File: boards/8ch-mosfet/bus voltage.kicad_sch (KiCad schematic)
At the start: 6 parts, among them U4 MCP3221A0T

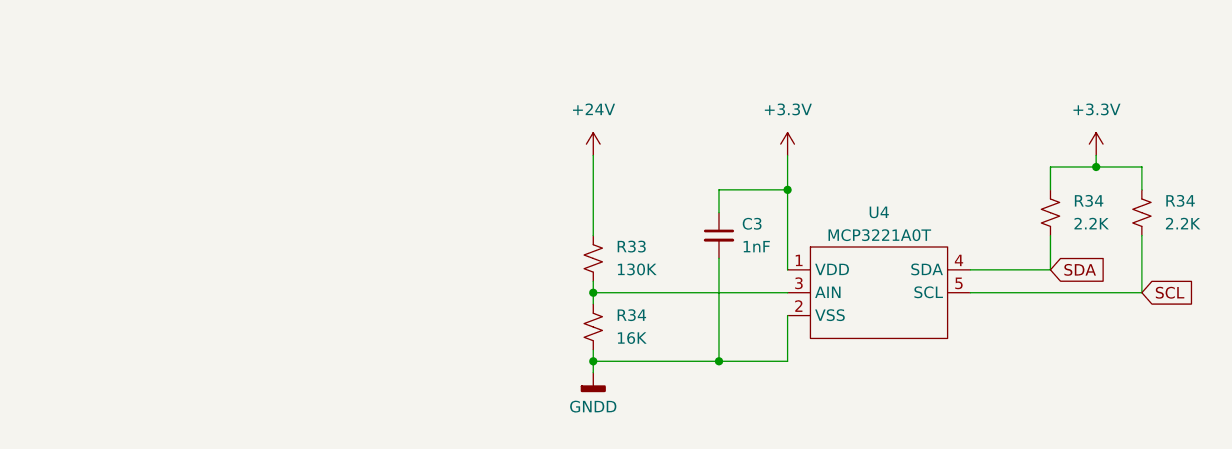
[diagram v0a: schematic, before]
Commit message: updated the adc schematic a bit
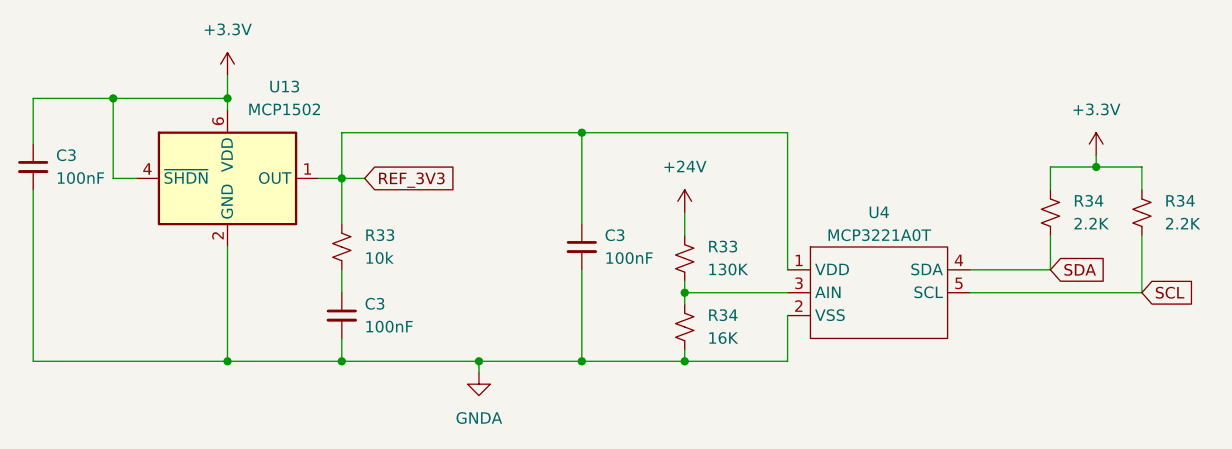
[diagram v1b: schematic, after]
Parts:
- added C3 (x2): 100nF, Capacitor_SMD:C_0805_2012Metric_Pad1.18x1.45mm_HandSolder, symbol Device:C_Small
- added R33: 10k, Resistor_SMD:R_0805_2012Metric_Pad1.20x1.40mm_HandSolder, symbol Device:R_Small_US
- added U13: MCP1502, Package_TO_SOT_SMD:SOT-23-6, symbol Reference_Voltage:MCP1501-30xCH
- C3: value 1nF -> 100nF
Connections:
- net +3.3V: now also C3.1, U13.4 (~{SHDN}), U13.6 (VDD); no longer C3.1, U4.1 (VDD)
- net GNDD renamed GNDA
- net GNDA: now also C3.2, C3.2, U13.2 (GND), U13.3 (GND), U13.5 (GND)
- new net: C3.1, R33.1
- new net REF_3V3: C3.1, R33.2, U13.1 (OUT), U4.1 (VDD)
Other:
- moved on the sheet: C3, R33, R34

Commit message: upgraded the i2c/serial connectors + power based on the sailor hat schematic
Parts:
- removed R34 (x2): 2.2K, Resistor_SMD:R_0805_2012Metric_Pad1.20x1.40mm_HandSolder, symbol Device:R_Small_US
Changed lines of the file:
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@@
   (junction (at 123.19 102.87) (diameter 0) (color 0 0 0 0)
   )
-  (junction (at 168.91 81.28) (diameter 0) (color 0 0 0 0)
-  )
   (junction (at 72.39 102.87) (diameter 0) (color 0 0 0 0)
   )
   (junction (at 72.39 73.66) (diameter 0) (color 0 0 0 0)
   )
-  (junction (at 111.76 77.47) (diameter 0) (color 0 0 0 0)
+  (junction (at 111.76 73.66) (diameter 0) (color 0 0 0 0)
   )
   (junction (at 85.09 102.87) (diameter 0) (color 0 0 0 0)
@@
     (stroke (width 0) (type default))
   )
-  (wire (pts (xy 163.83 81.28) (xy 168.91 81.28))
-    (stroke (width 0) (type default))
-  )
-  (wire (pts (xy 111.76 77.47) (xy 111.76 87.63))
-    (stroke (width 0) (type default))
-  )
   (wire (pts (xy 123.19 95.25) (xy 134.62 95.25))
     (stroke (width 0) (type default))
@@
     (stroke (width 0) (type default))
   )
-  (wire (pts (xy 134.62 77.47) (xy 134.62 92.71))
+  (wire (pts (xy 134.62 73.66) (xy 134.62 92.71))
     (stroke (width 0) (type default))
   )
@@
     (stroke (width 0) (type default))
   )
-  (wire (pts (xy 173.99 83.82) (xy 173.99 81.28))
-    (stroke (width 0) (type default))
-  )
   (wire (pts (xy 85.09 92.71) (xy 85.09 95.25))
     (stroke (width 0) (type default))
@@
     (stroke (width 0) (type default))
   )
-  (wire (pts (xy 163.83 88.9) (xy 163.83 92.71))
-    (stroke (width 0) (type default))
-  )
   (wire (pts (xy 72.39 90.17) (xy 72.39 102.87))
     (stroke (width 0) (type default))
   )
-  (wire (pts (xy 163.83 83.82) (xy 163.83 81.28))
-    (stroke (width 0) (type default))
-  )
   (wire (pts (xy 100.33 102.87) (xy 111.76 102.87))
     (stroke (width 0) (type default))
@@
     (stroke (width 0) (type default))
   )
-  (wire (pts (xy 173.99 88.9) (xy 173.99 95.25))
-    (stroke (width 0) (type default))
-  )
   (wire (pts (xy 72.39 73.66) (xy 59.69 73.66))
     (stroke (width 0) (type default))
@@
     (stroke (width 0) (type default))
   )
-  (wire (pts (xy 154.94 95.25) (xy 173.99 95.25))
+  (wire (pts (xy 154.94 95.25) (xy 158.75 95.25))
     (stroke (width 0) (type default))
   )
@@
     (stroke (width 0) (type default))
   )
-  (wire (pts (xy 111.76 77.47) (xy 134.62 77.47))
+  (wire (pts (xy 111.76 73.66) (xy 134.62 73.66))
     (stroke (width 0) (type default))
   )
@@
     (stroke (width 0) (type default))
   )
-  (wire (pts (xy 85.09 77.47) (xy 111.76 77.47))
-    (stroke (width 0) (type default))
-  )
-  (wire (pts (xy 168.91 81.28) (xy 168.91 80.01))
-    (stroke (width 0) (type default))
-  )
-  (wire (pts (xy 173.99 81.28) (xy 168.91 81.28))
+  (wire (pts (xy 85.09 73.66) (xy 111.76 73.66))
     (stroke (width 0) (type default))
   )
@@
     (stroke (width 0) (type default))
   )
-  (wire (pts (xy 85.09 82.55) (xy 85.09 77.47))
+  (wire (pts (xy 85.09 82.55) (xy 85.09 73.66))
     (stroke (width 0) (type default))
   )
@@
     (stroke (width 0) (type default))
   )
-  (wire (pts (xy 154.94 92.71) (xy 163.83 92.71))
+  (wire (pts (xy 154.94 92.71) (xy 158.75 92.71))
     (stroke (width 0) (type default))
   )
@@
   )
   (wire (pts (xy 59.69 73.66) (xy 50.8 73.66))
+    (stroke (width 0) (type default))
+  )
+  (wire (pts (xy 111.76 73.66) (xy 111.76 87.63))
     (stroke (width 0) (type default))
   )
@@
     )
   )
-  (global_label "SDA" (shape input) (at 163.83 92.71 0) (fields_autoplaced)
+  (global_label "SDA" (shape input) (at 158.75 92.71 0) (fields_autoplaced)
     (effects (font (size 1.27 1.27)) (justify left))
-    (property "Intersheetrefs" "${INTERSHEET_REFS}" (at 170.3833 92.71 0)
+    (property "Intersheetrefs" "${INTERSHEET_REFS}" (at 165.3033 92.71 0)
       (effects (font (size 1.27 1.27)) (justify left) hide)
     )
   )
-  (global_label "SCL" (shape input) (at 173.99 95.25 0) (fields_autoplaced)
+  (global_label "SCL" (shape input) (at 158.75 95.25 0) (fields_autoplaced)
     (effects (font (size 1.27 1.27)) (justify left))
-    (property "Intersheetrefs" "${INTERSHEET_REFS}" (at 180.4828 95.25 0)
+    (property "Intersheetrefs" "${INTERSHEET_REFS}" (at 165.2428 95.25 0)
       (effects (font (size 1.27 1.27)) (justify left) hide)
-    )
-  )
-  (symbol (lib_id "Device:R_Small_US") (at 163.83 86.36 180) (unit 1)
-    (in_bom yes) (on_board yes) (dnp no) (fields_autoplaced)
-    (property "Reference" "R34" (at 166.37 85.09 0)
-      (effects (font (size 1.27 1.27)) (justify right))
-    )
-    (property "Value" "2.2K" (at 166.37 87.63 0)
-      (effects (font (size 1.27 1.27)) (justify right))
-    )
-    (property "Footprint" "Resistor_SMD:R_0805_2012Metric_Pad1.20x1.40mm_HandSolder" (at 163.83 86.36 0)
-      (effects (font (size 1.27 1.27)) hide)
-    )
-    (property "Datasheet" "~" (at 163.83 86.36 0)
-      (effects (font (size 1.27 1.27)) hide)
-    )
-    (property "Vendor" "652-CR0805JW-104ELF" (at 163.83 86.36 0)
-      (effects (font (size 1.27 1.27)) hide)
-    )
-    (pin "1")
-    (pin "2")
-    (instances
-      (project "8ch-mosfet"
-        (path "/c83c6236-96e9-46ad-9d7a-9e2efa4a7966"
-          (reference "R34") (unit 1)
-        )
-        (path "/c83c6236-96e9-46ad-9d7a-9e2efa4a7966/0eec6767-666b-42c0-ba36-2a83c9caeade"
-          (reference "R4") (unit 1)
-        )
-        (path "/c83c6236-96e9-46ad-9d7a-9e2efa4a7966/ccdb1c25-8d0f-4f30-ab70-bbc1ecf3f6f7"
-          (reference "R8") (unit 1)
-        )
-        (path "/c83c6236-96e9-46ad-9d7a-9e2efa4a7966/1e692482-a022-407a-8cb5-d9a3b23521a6"
-          (reference "R12") (unit 1)
-        )
-        (path "/c83c6236-96e9-46ad-9d7a-9e2efa4a7966/5952e660-2bb6-45cf-b9ea-f7a7c2d0954e"
-          (reference "R16") (unit 1)
-        )
-        (path "/c83c6236-96e9-46ad-9d7a-9e2efa4a7966/772d44f5-8758-48db-a140-72ed8e75e88c"
-          (reference "R20") (unit 1)
-        )
-        (path "/c83c6236-96e9-46ad-9d7a-9e2efa4a7966/424e7b24-5644-46f2-85bb-1e459a343705"
-          (reference "R24") (unit 1)
-        )
-        (path "/c83c6236-96e9-46ad-9d7a-9e2efa4a7966/4c1df725-56ca-4be4-8107-a39054acbca4"
-          (reference "R28") (unit 1)
-        )
-        (path "/c83c6236-96e9-46ad-9d7a-9e2efa4a7966/a8a81147-5613-4820-beb3-a7ca76d0db8e"
-          (reference "R32") (unit 1)
-        )
-        (path "/c83c6236-96e9-46ad-9d7a-9e2efa4a7966/b87f80e1-ecbd-4ee0-be26-4b252158928b"
-          (reference "R39") (unit 1)
-        )
-      )
     )
   )
@@
         (path "/c83c6236-96e9-46ad-9d7a-9e2efa4a7966/b87f80e1-ecbd-4ee0-be26-4b252158928b"
           (reference "R41") (unit 1)
-        )
-      )
-    )
-  )
-  (symbol (lib_id "Device:R_Small_US") (at 173.99 86.36 180) (unit 1)
-    (in_bom yes) (on_board yes) (dnp no) (fields_autoplaced)
-    (property "Reference" "R34" (at 176.53 85.09 0)
-      (effects (font (size 1.27 1.27)) (justify right))
-    )
-    (property "Value" "2.2K" (at 176.53 87.63 0)
-      (effects (font (size 1.27 1.27)) (justify right))
-    )
-    (property "Footprint" "Resistor_SMD:R_0805_2012Metric_Pad1.20x1.40mm_HandSolder" (at 173.99 86.36 0)
-      (effects (font (size 1.27 1.27)) hide)
-    )
-    (property "Datasheet" "~" (at 173.99 86.36 0)
-      (effects (font (size 1.27 1.27)) hide)
-    )
-    (property "Vendor" "652-CR0805JW-104ELF" (at 173.99 86.36 0)
-      (effects (font (size 1.27 1.27)) hide)
-    )
-    (pin "1")
-    (pin "2")
-    (instances
-      (project "8ch-mosfet"
-        (path "/c83c6236-96e9-46ad-9d7a-9e2efa4a7966"
-          (reference "R34") (unit 1)
-        )
-        (path "/c83c6236-96e9-46ad-9d7a-9e2efa4a7966/0eec6767-666b-42c0-ba36-2a83c9caeade"
-          (reference "R4") (unit 1)
-        )
-        (path "/c83c6236-96e9-46ad-9d7a-9e2efa4a7966/ccdb1c25-8d0f-4f30-ab70-bbc1ecf3f6f7"
-          (reference "R8") (unit 1)
-        )
-        (path "/c83c6236-96e9-46ad-9d7a-9e2efa4a7966/1e692482-a022-407a-8cb5-d9a3b23521a6"
-          (reference "R12") (unit 1)
-        )
-        (path "/c83c6236-96e9-46ad-9d7a-9e2efa4a7966/5952e660-2bb6-45cf-b9ea-f7a7c2d0954e"
-          (reference "R16") (unit 1)
-        )
-        (path "/c83c6236-96e9-46ad-9d7a-9e2efa4a7966/772d44f5-8758-48db-a140-72ed8e75e88c"
-          (reference "R20") (unit 1)
-        )
-        (path "/c83c6236-96e9-46ad-9d7a-9e2efa4a7966/424e7b24-5644-46f2-85bb-1e459a343705"
-          (reference "R24") (unit 1)
-        )
-        (path "/c83c6236-96e9-46ad-9d7a-9e2efa4a7966/4c1df725-56ca-4be4-8107-a39054acbca4"
-          (reference "R28") (unit 1)
-        )
-        (path "/c83c6236-96e9-46ad-9d7a-9e2efa4a7966/a8a81147-5613-4820-beb3-a7ca76d0db8e"
-          (reference "R32") (unit 1)
-        )
-        (path "/c83c6236-96e9-46ad-9d7a-9e2efa4a7966/b87f80e1-ecbd-4ee0-be26-4b252158928b"
-          (reference "R40") (unit 1)
         )
       )
@@
         )
       )
-    )
-  )
-  (symbol (lib_id "power:+3.3V") (at 168.91 80.01 0) (unit 1)
-    (in_bom yes) (on_board yes) (dnp no) (fields_autoplaced)
-    (property "Reference" "#PWR02" (at 168.91 83.82 0)
-      (effects (font (size 1.27 1.27)) hide)
-    )
-    (property "Value" "+3.3V" (at 168.91 74.93 0)
-      (effects (font (size 1.27 1.27)))
-    )
-    (property "Footprint" "" (at 168.91 80.01 0)
-      (effects (font (size 1.27 1.27)) hide)
-    )
-    (property "Datasheet" "" (at 168.91 80.01 0)
-      (effects (font (size 1.27 1.27)) hide)
-    )
-    (pin "1")
-    (instances
-      (project "8ch-mosfet"
-        (path "/c83c6236-96e9-46ad-9d7a-9e2efa4a7966"
-          (reference "#PWR02") (unit 1)
-        )
-        (path "/c83c6236-96e9-46ad-9d7a-9e2efa4a7966/b87f80e1-ecbd-4ee0-be26-4b252158928b"
-          (reference "#PWR068") (unit 1)
-        )
-      )

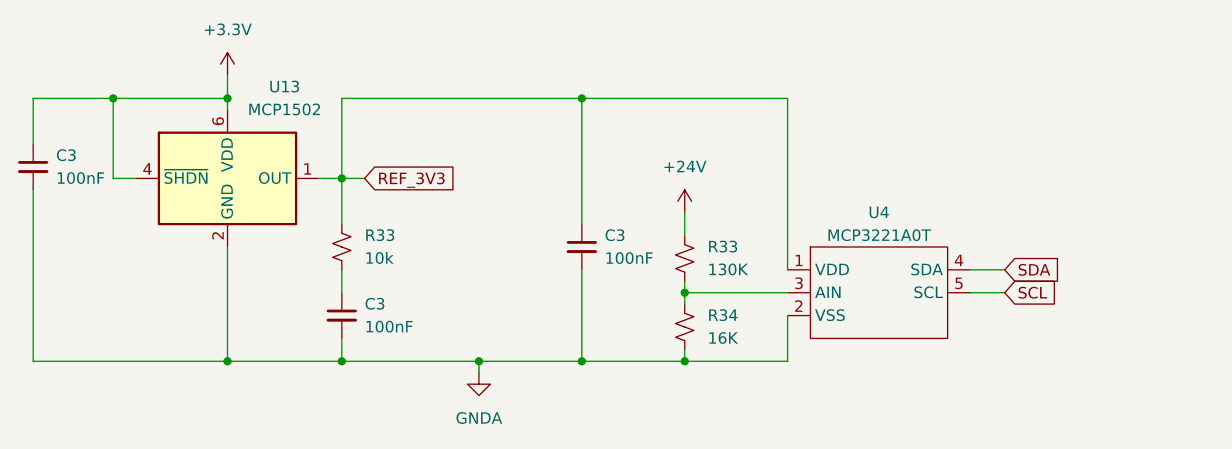
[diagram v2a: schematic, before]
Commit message: silkscreen updated, drc passed.  yay
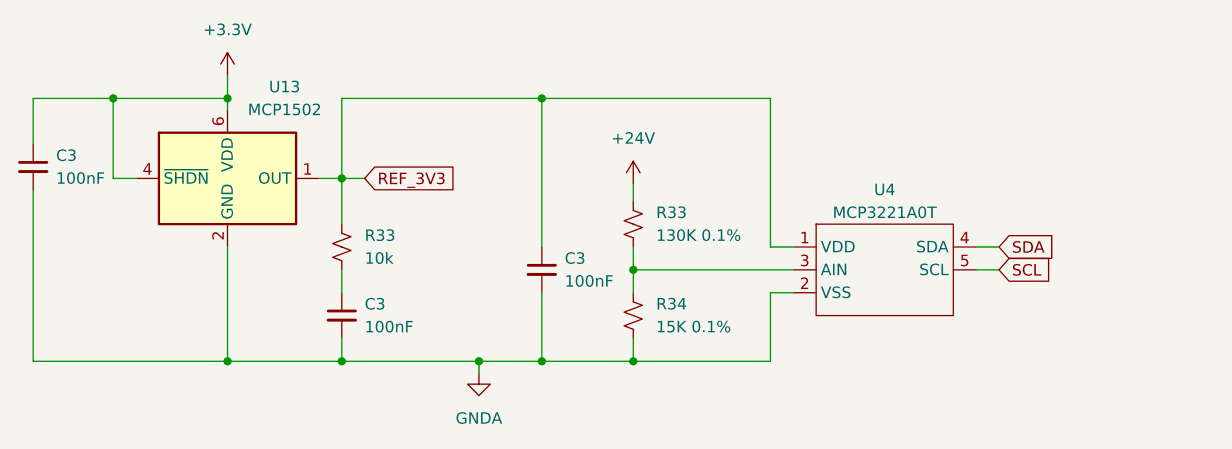
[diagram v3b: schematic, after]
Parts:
- R33: value 130K -> 130K 0.1%; Vendor 652-CR0805JW-104ELF -> (none)
- R34: value 16K -> 15K 0.1%; Vendor 652-CR0805JW-104ELF -> (none)
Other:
- moved on the sheet: C3, R33, R34, U4
